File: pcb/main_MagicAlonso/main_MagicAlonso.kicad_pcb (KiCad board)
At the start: 2 copper layers, 3 parts

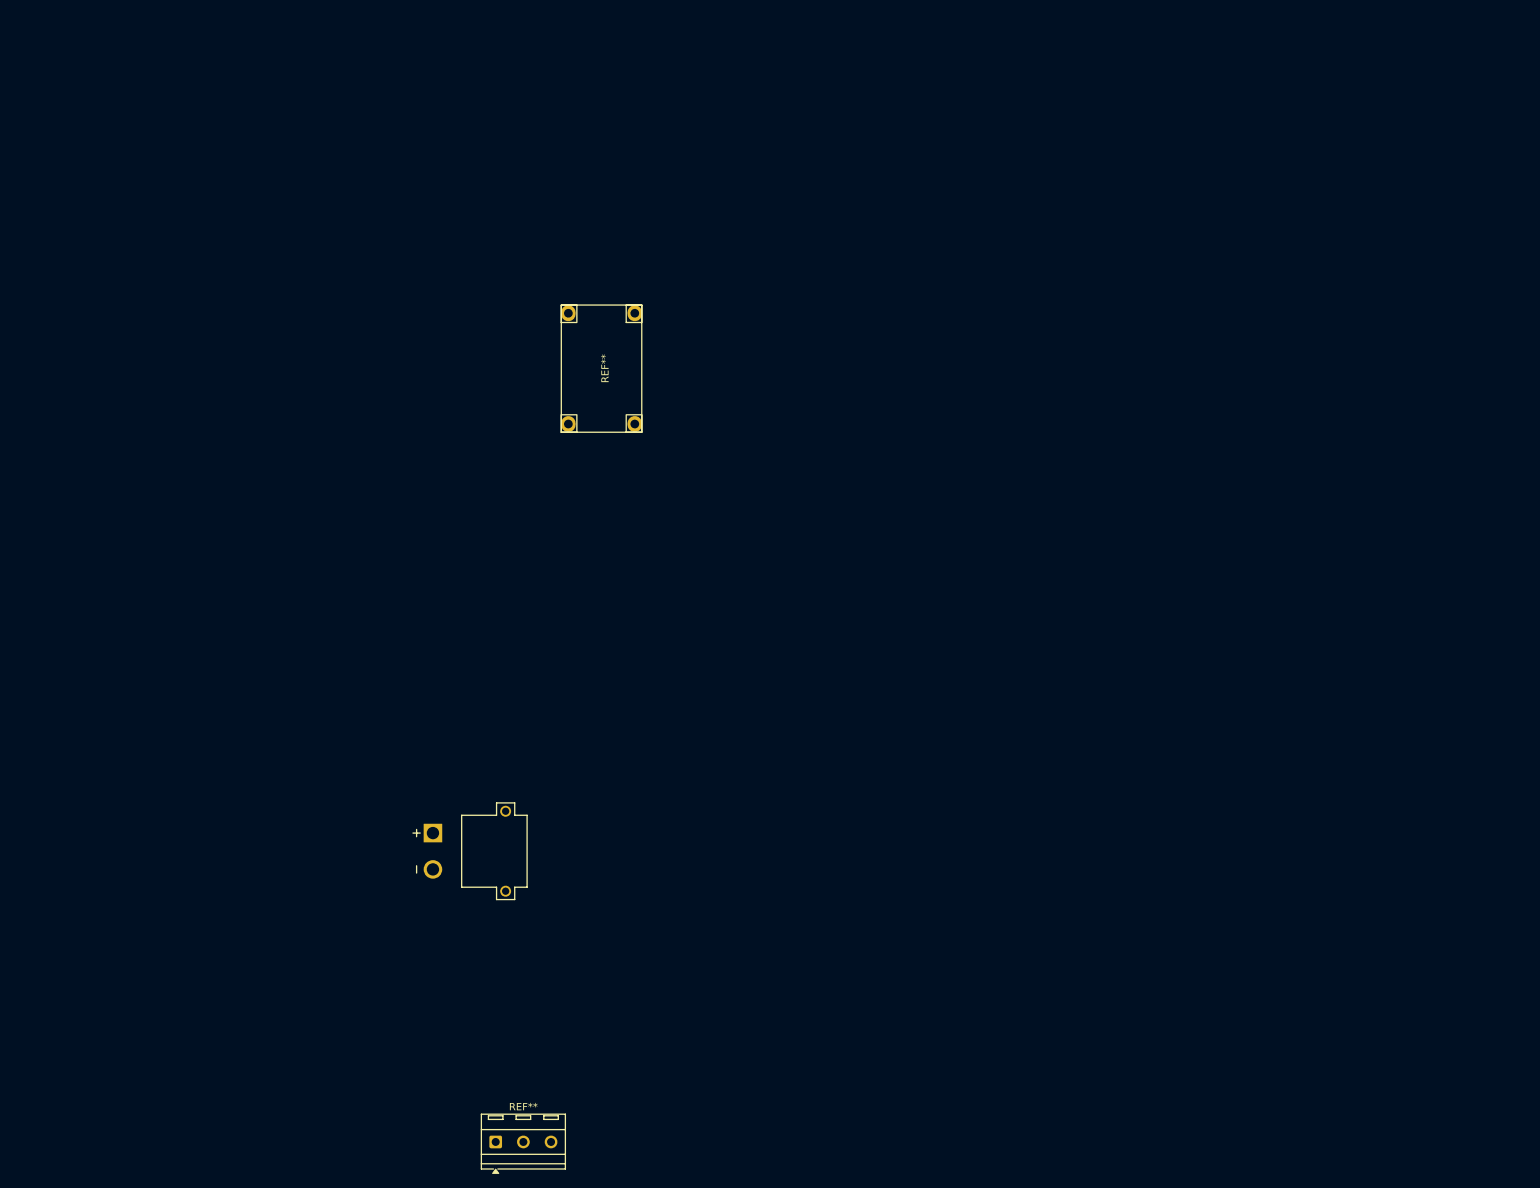
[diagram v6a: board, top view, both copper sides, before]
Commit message: pcb footprint added
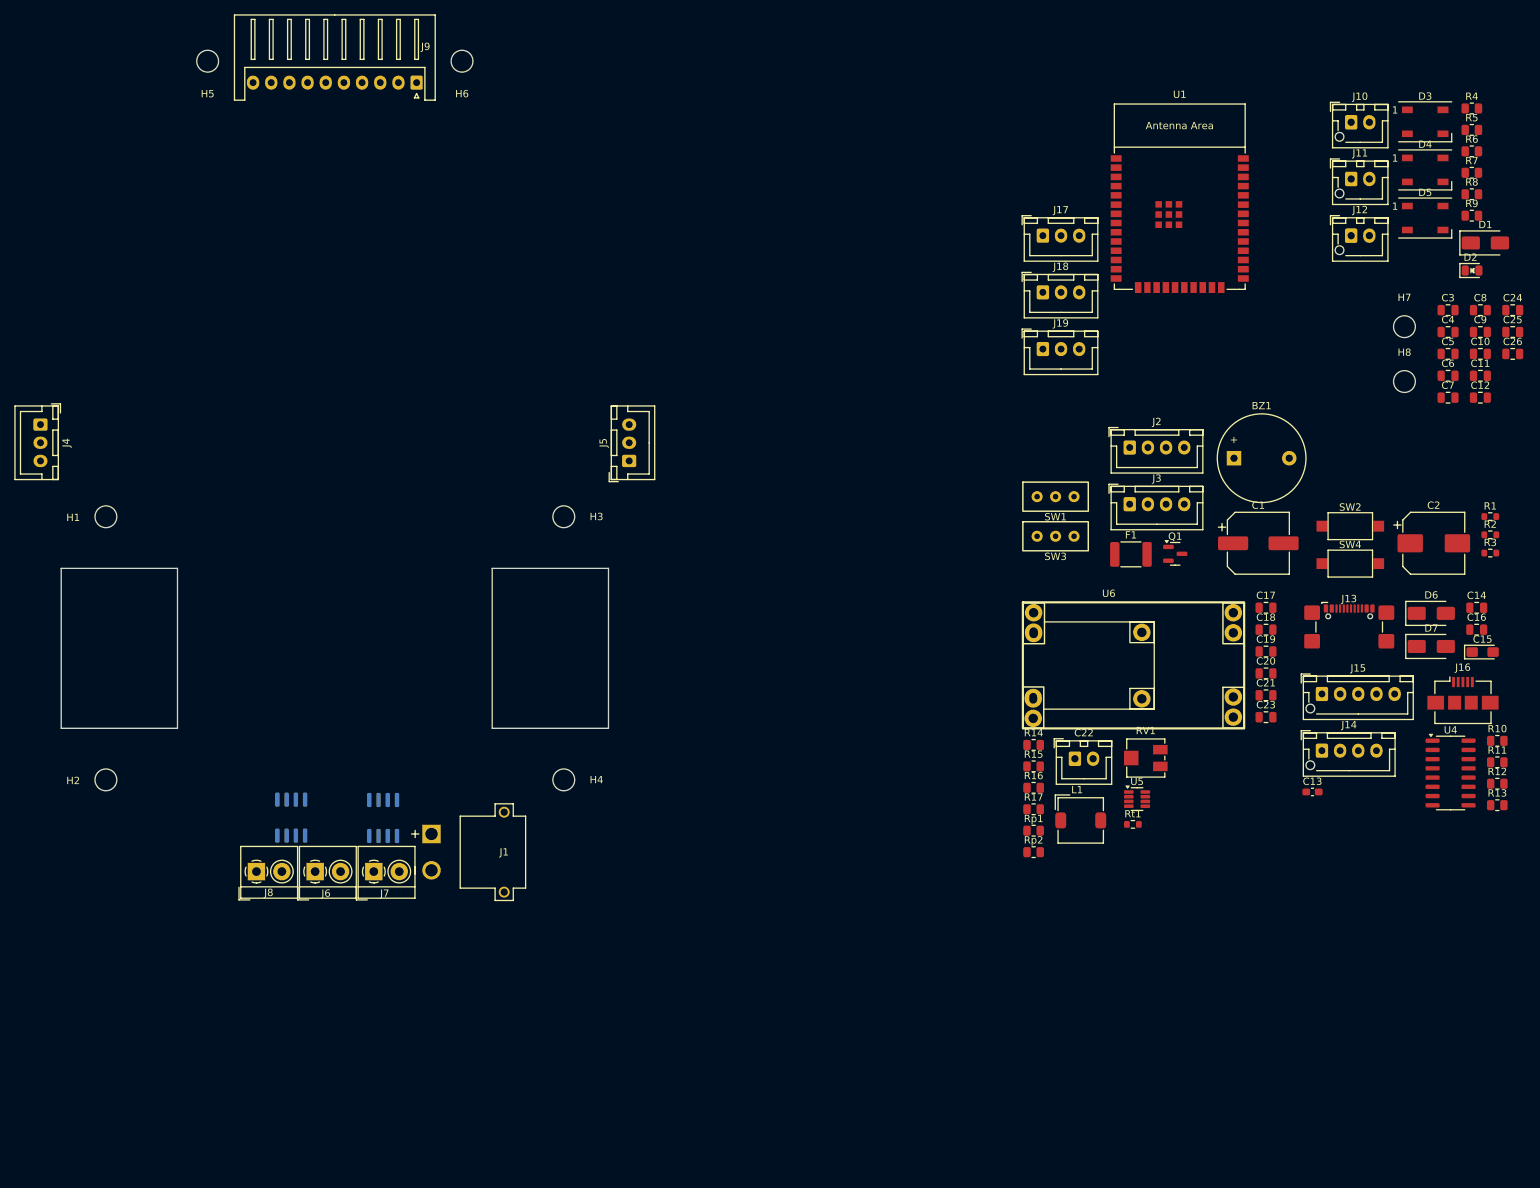
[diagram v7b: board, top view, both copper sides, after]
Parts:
- removed REF**: TerminalBlock_MetzConnect_Type086_RT03403HBLC_1x03_P3.81mm_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, TerminalBlock_MetzConnect:TerminalBlock_MetzConnect_Type086_RT03403HBLC_1x03_P3.81mm_Horizontal
- removed REF**: Mini360, MixLib:Mini360_step-down
- removed REF**: AMASS_XT30PW-M, MixLib:XT30PW-M
- added BZ1: Buzzer, Buzzer_Beeper:Buzzer_12x9.5RM7.6, F.Cu at (230.2, 177.1)
- added C1: 330uF, Capacitor_SMD:CP_Elec_8x11.9, F.Cu at (233.6, 188.8)
- added C10: 10nF, Capacitor_SMD:C_0805_2012Metric, F.Cu at (264.1, 162.8)
- added C11: 1uF, Capacitor_SMD:C_0805_2012Metric, F.Cu at (264.1, 165.8)
- added C12: 100nF, Capacitor_SMD:C_0805_2012Metric, F.Cu at (264.1, 168.8)
- added C13: 1uF, Capacitor_SMD:C_0603_1608Metric_Pad1.08x0.95mm_HandSolder, F.Cu at (241.0, 223.0)
- added C14: 100nF, Capacitor_SMD:C_0805_2012Metric, F.Cu at (263.6, 197.7)
- added C15: 10uF, Capacitor_Tantalum_SMD:CP_EIA-3216-10_Kemet-I_Pad1.58x1.35mm_HandSolder, F.Cu at (264.4, 203.8)
- added C16: 100nF, Capacitor_SMD:C_0805_2012Metric, F.Cu at (263.6, 200.7)
- added C17: 22uF, Capacitor_SMD:C_0805_2012Metric, F.Cu at (234.6, 197.7)
- added C18: 100nF, Capacitor_SMD:C_0805_2012Metric, F.Cu at (234.6, 200.7)
- added C19: 100nF, Capacitor_SMD:C_0805_2012Metric, F.Cu at (234.6, 203.7)
- added C2: 100uF, Capacitor_SMD:CP_Elec_8x10, F.Cu at (257.7, 188.8)
- added C20: 22uF, Capacitor_SMD:C_0805_2012Metric, F.Cu at (234.6, 206.7)
- added C21: 22uF, Capacitor_SMD:C_0805_2012Metric, F.Cu at (234.6, 209.7)
- added C22: 47uF, Connector_JST:JST_XH_B2B-XH-A_1x02_P2.50mm_Vertical, F.Cu at (208.3, 218.5)
- added C23: 100nF, Capacitor_SMD:C_0805_2012Metric, F.Cu at (234.6, 212.8)
- added C24: 100nF, Capacitor_SMD:C_0805_2012Metric, F.Cu at (268.6, 156.8)
- added C25: 100nF, Capacitor_SMD:C_0805_2012Metric, F.Cu at (268.6, 159.8)
- added C26: 100nF, Capacitor_SMD:C_0805_2012Metric, F.Cu at (268.6, 162.8)
- added C3: 1uF, Capacitor_SMD:C_0805_2012Metric, F.Cu at (259.7, 156.8)
- added C4: 100nF, Capacitor_SMD:C_0805_2012Metric, F.Cu at (259.7, 159.8)
- added C5: 100nF, Capacitor_SMD:C_0805_2012Metric, F.Cu at (259.7, 162.8)
- added C6: 100nF, Capacitor_SMD:C_0805_2012Metric, F.Cu at (259.7, 165.8)
- added C7: 100nF, Capacitor_SMD:C_0805_2012Metric, F.Cu at (259.7, 168.8)
- added C8: 100nF, Capacitor_SMD:C_0805_2012Metric, F.Cu at (264.1, 156.8)
- added C9: 10nF, Capacitor_SMD:C_0805_2012Metric, F.Cu at (264.1, 159.8)
- added D1: SS14, Diode_SMD:D_SMA, F.Cu at (264.8, 147.5)
- added D2: LED_On, MixLib:LED_0805_2012Metric, F.Cu at (262.8, 151.3)
- added D3: WS2812B, LED_SMD:LED_WS2812B_PLCC4_5.0x5.0mm_P3.2mm, F.Cu at (256.5, 130.8)
- added D4: WS2812B, LED_SMD:LED_WS2812B_PLCC4_5.0x5.0mm_P3.2mm, F.Cu at (256.5, 137.5)
- added D5: WS2812B, LED_SMD:LED_WS2812B_PLCC4_5.0x5.0mm_P3.2mm, F.Cu at (256.5, 144.1)
- added D6: SS14, Diode_SMD:D_SMA, F.Cu at (257.4, 198.5)
- added D7: SS14, Diode_SMD:D_SMA, F.Cu at (257.4, 203.0)
- added F1: 300mA, Fuse:Fuse_1812_4532Metric_Pad1.30x3.40mm_HandSolder, F.Cu at (216.0, 190.4)
- added H1: M3, MountingHole:MountingHole_3mm, F.Cu at (75.0, 185.2)
- added H2: M3, MountingHole:MountingHole_3mm, F.Cu at (75.0, 221.4)
- added H3: M3, MountingHole:MountingHole_3mm, F.Cu at (138.0, 185.2)
- added H4: M3, MountingHole:MountingHole_3mm, F.Cu at (138.0, 221.4)
- added H5: M3, MountingHole:MountingHole_3mm, F.Cu at (89.0, 122.5)
- added H6: M3, MountingHole:MountingHole_3mm, F.Cu at (124.0, 122.5)
- added H7: M3, MountingHole:MountingHole_3mm, F.Cu at (253.7, 159.0)
- added H8: M3, MountingHole:MountingHole_3mm, F.Cu at (253.7, 166.6)
- added J1: XT30PW-M, MixLib:XT30PW-M, F.Cu at (129.8, 231.3)
- added J10: ESC1, Connector_JST:JST_XH_B2B-XH-AM_1x02_P2.50mm_Vertical, F.Cu at (246.3, 130.9)
- added J11: ESC2, Connector_JST:JST_XH_B2B-XH-AM_1x02_P2.50mm_Vertical, F.Cu at (246.3, 138.7)
- added J12: ESC3, Connector_JST:JST_XH_B2B-XH-AM_1x02_P2.50mm_Vertical, F.Cu at (246.3, 146.5)
- added J13: USB_C_Receptacle_USB2.0_16P, Connector_USB:USB_C_Receptacle_GCT_USB4110, F.Cu at (246.1, 201.5)
- added J14: UART_Out, Connector_JST:JST_XH_B4B-XH-AM_1x04_P2.50mm_Vertical, F.Cu at (242.3, 217.4)
- added J15: USB_Out, Connector_JST:JST_XH_B5B-XH-AM_1x05_P2.50mm_Vertical, F.Cu at (242.3, 209.6)
- added J16: USB_B_Micro, Connector_USB:USB_Micro-B_Amphenol_10104110_Horizontal, F.Cu at (261.7, 209.5)
- added J17: aux0, Connector_JST:JST_XH_B3B-XH-A_1x03_P2.50mm_Vertical, F.Cu at (203.9, 146.5)
- added J18: aux2, Connector_JST:JST_XH_B3B-XH-A_1x03_P2.50mm_Vertical, F.Cu at (203.9, 154.3)
- added J19: aux1, Connector_JST:JST_XH_B3B-XH-A_1x03_P2.50mm_Vertical, F.Cu at (203.9, 162.1)
- added J2: MPU6050, Connector_JST:JST_XH_B4B-XH-A_1x04_P2.50mm_Vertical, F.Cu at (215.9, 175.7)
- added J3: OLED, Connector_JST:JST_XH_B4B-XH-A_1x04_P2.50mm_Vertical, F.Cu at (215.9, 183.5)
- added J4: Encoder1, Connector_JST:JST_XH_B3B-XH-A_1x03_P2.50mm_Vertical, F.Cu at (66.0, 172.5)
- added J5: Encoder2, Connector_JST:JST_XH_B3B-XH-A_1x03_P2.50mm_Vertical, F.Cu at (147.0, 177.5)
- added J6: ESC1_Vb, TerminalBlock_4Ucon:TerminalBlock_4Ucon_1x02_P3.50mm_Horizontal, F.Cu at (103.8, 234.0)
- added J7: ESC2_Vb, TerminalBlock_4Ucon:TerminalBlock_4Ucon_1x02_P3.50mm_Horizontal, F.Cu at (111.9, 234.0)
- added J8: ESC3_Vb, TerminalBlock_4Ucon:TerminalBlock_4Ucon_1x02_P3.50mm_Horizontal, F.Cu at (95.7, 234.0)
- added J9: Sensors, Connector_JST:JST_XH_S10B-XH-A_1x10_P2.50mm_Horizontal, F.Cu at (117.8, 125.5)
- added L1: 6.8uH, Inductor_SMD:L_TDK_SLF6025, F.Cu at (209.1, 227.0)
- added Q1: IRLML2502, Package_TO_SOT_SMD:SOT-23, F.Cu at (222.1, 190.3)
- added R1: 1k, Resistor_SMD:R_0603_1608Metric, F.Cu at (265.5, 185.2)
- added R10: 10k, Resistor_SMD:R_0805_2012Metric, F.Cu at (266.4, 216.0)
- added R11: 10k, Resistor_SMD:R_0805_2012Metric, F.Cu at (266.4, 219.0)
- added R12: 10k, Resistor_SMD:R_0805_2012Metric, F.Cu at (266.4, 221.9)
- added R13: 10k, Resistor_SMD:R_0805_2012Metric, F.Cu at (266.4, 224.9)
- added R14: 20, Resistor_SMD:R_0805_2012Metric, F.Cu at (202.6, 216.6)
- added R15: 100k, Resistor_SMD:R_0805_2012Metric, F.Cu at (202.6, 219.5)
- added R16: 10k, Resistor_SMD:R_0805_2012Metric, F.Cu at (202.6, 222.5)
- added R17: 10k, Resistor_SMD:R_0805_2012Metric, F.Cu at (202.6, 225.4)
- added R2: 10k, Resistor_SMD:R_0603_1608Metric, F.Cu at (265.5, 187.7)
- added R3: 10k, Resistor_SMD:R_0603_1608Metric, F.Cu at (265.5, 190.2)
- added R4: 330, Resistor_SMD:R_0805_2012Metric, F.Cu at (262.9, 129.0)
- added R5: 100, Resistor_SMD:R_0805_2012Metric, F.Cu at (262.9, 132.0)
- added R6: 100, Resistor_SMD:R_0805_2012Metric, F.Cu at (262.9, 134.9)
- added R7: 100, Resistor_SMD:R_0805_2012Metric, F.Cu at (262.9, 137.9)
- added R8: 330, Resistor_SMD:R_0805_2012Metric, F.Cu at (262.9, 140.8)
- added R9: 10k, Resistor_SMD:R_0805_2012Metric, F.Cu at (262.9, 143.8)
- added RV1: Pot, Potentiometer_SMD:Potentiometer_Vishay_TS53YJ_Vertical, F.Cu at (218.1, 218.4)
- added Rp1: 47k, Resistor_SMD:R_0805_2012Metric, F.Cu at (202.6, 228.4)
- added Rp2: 100k, Resistor_SMD:R_0805_2012Metric, F.Cu at (202.6, 231.3)
- added Rt1: 33k, Resistor_SMD:R_0603_1608Metric, F.Cu at (216.3, 227.5)
- added SW1: Power_SW, MixLib:SW_Slide-03_P2.54_L9_W4_H7, F.Cu at (205.7, 182.4)
- added SW2: EN_Push, Button_Switch_SMD:SW_SPST_CK_RS282G05A3, F.Cu at (246.2, 186.5)
- added SW3: Boot_SW, MixLib:SW_Slide-03_P2.54_L9_W4_H7, F.Cu at (205.7, 187.9)
- added SW4: BUTTON_Push, Button_Switch_SMD:SW_SPST_CK_RS282G05A3, F.Cu at (246.2, 191.6)
- added U1: ESP32-WROOM-32E, PCM_Espressif:ESP32-WROOM-32E, F.Cu at (222.8, 142.9)
- added U2: ACS712-30A, Package_SO:SOIC-8_3.9x4.9mm_P1.27mm, B.Cu at (113.1, 226.6)
- added U3: ACS712-20A, Package_SO:SOIC-8_3.9x4.9mm_P1.27mm, B.Cu at (100.5, 226.6)
- added U4: CH340C, Package_SO:SOIC-16_3.9x9.9mm_P1.27mm, F.Cu at (260.0, 220.4)
- added U5: MP2315, Package_TO_SOT_SMD:TSOT-23-8, F.Cu at (216.9, 224.0)
- added U6: Mini360-MP4560, MixLib:Mix_Mini360-MP4560, F.Cu at (215.8, 205.5)
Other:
- board outline added: 75.3 x 22 mm
- board text added: "BLS 2130 55A 4IN1 ESC"

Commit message: pcb components & label fixes
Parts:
- removed U5: MP2315, Package_TO_SOT_SMD:TSOT-23-8
- added ST1: MP2315, Package_TO_SOT_SMD:TSOT-23-8, F.Cu at (252.8, 135.2)
- C1: footprint Capacitor_SMD:CP_Elec_8x11.9 -> Capacitor_THT:CP_Radial_D8.0mm_P3.80mm
- C15: footprint Capacitor_Tantalum_SMD:CP_EIA-3216-10_Kemet-I_Pad1.58x1.35mm_HandSolder -> Capacitor_Tantalum_SMD:CP_EIA-3216-10_Kemet-I_HandSolder
- C2: footprint Capacitor_SMD:CP_Elec_8x10 -> Capacitor_SMD:CP_Elec_6.3x5.4
- C22: footprint Connector_JST:JST_XH_B2B-XH-A_1x02_P2.50mm_Vertical -> Capacitor_SMD:CP_Elec_6.3x5.4
- J10, J11, J12: footprint Connector_JST:JST_XH_B2B-XH-AM_1x02_P2.50mm_Vertical -> Connector_JST:JST_XH_B2B-XH-A_1x02_P2.50mm_Vertical
- J14: footprint Connector_JST:JST_XH_B4B-XH-AM_1x04_P2.50mm_Vertical -> Connector_JST:JST_XH_B4B-XH-A_1x04_P2.50mm_Vertical
- J15: footprint Connector_JST:JST_XH_B5B-XH-AM_1x05_P2.50mm_Vertical -> Connector_PinSocket_2.54mm:PinSocket_1x05_P2.54mm_Vertical
- J6: value ESC1_Vb -> ESC1_VM
- J7: value ESC2_Vb -> ESC2_VM
- J8: value ESC3_Vb -> ESC3_VM
- U6: value Mini360-MP4560 -> Mini360; footprint MixLib:Mix_Mini360-MP4560 -> MixLib:Mini360_step-down
- moved C5 242.1 mm to (18.1, 147.2)
- moved C6 242.1 mm to (18.1, 150.3)
- moved C7 242.1 mm to (18.1, 153.3)
- moved C10 242.1 mm to (22.6, 147.2)
- moved C8 242.1 mm to (22.6, 141.2)
- moved C9 242.1 mm to (22.6, 144.2)
- moved R1 240.1 mm to (26.0, 168.2)
- moved R2 240.1 mm to (26.0, 170.7)
- moved R3 240.1 mm to (26.0, 173.2)
- moved C4 198.7 mm to (61.2, 170.4), turned to -90 degrees
- moved C3 196.9 mm to (63.2, 170.4), turned to -90 degrees
- moved C12 171.9 mm to (96.5, 130.4), turned to 180 degrees
- moved SW2 171.6 mm to (75.4, 170.3), turned to 180 degrees
- moved C11 170.7 mm to (96.5, 133.4), turned to 180 degrees
- moved F1 168.5 mm to (49.8, 162.8), turned to -90 degrees
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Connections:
- net /CH340C/Vbus renamed /CH340C/VMus
- net /CH340C/VbusB renamed /CH340C/VMusB
- net /CH340C/VbusC renamed /CH340C/VMusC
- net /ESC1&2_Vb renamed /ESC1&2_VM
- net /ESC3_Vb renamed /ESC3_VM
- net Net-(U5-SW) renamed /StepDown_2315/SW
- net Net-(U5-VCC) renamed /StepDown_2315/VCC_MP
- C1 pad 1: /Vb -> /VM
- C15 pad 2: /Vusb -> /Vb
- C16 pad 2: /Vusb -> /Vb
- C17 pad 1: /Vusb -> /Vb
- C18 pad 1: /Vusb -> /Vb
- C2 pad 1: /Vb -> /VM
- C24 pad 1: +3.3V -> Net-(D3-VDD)
- C24 pad 2: Net-(D3-VDD) -> GND
- C25 pad 1: +3.3V -> Net-(D4-VDD)
- C25 pad 2: Net-(D4-VDD) -> GND
- C26 pad 1: +3.3V -> Net-(D5-VDD)
- C26 pad 2: Net-(D5-VDD) -> GND
- D1 pad 1: /Vusb -> /Vb
- D6 pad 1: /Vusb -> /Vb
- D7 pad 1: /Vusb -> /Vb
- J1 pad P: /Vb -> /VM
- R14 pad 2: Net-(U5-BST) -> /StepDown_2315/BST
- R15 pad 2: /Vusb -> /Vb
- R16 pad 1: Net-(U5-AAM) -> /StepDown_2315/AAM
- R4 pad 2: /Vb -> /VM
- Rt1 pad 1: Net-(U5-FB) -> /StepDown_2315/FB
- SW1 pad 1: /Vb -> /VM
- U2 pad 1: /Vb -> /VM
- U2 pad 2: /Vb -> /VM
- U3 pad 1: /Vb -> /VM
- U3 pad 2: /Vb -> /VM
- U6 pad 1: /Vusb -> /Vb
- U6 pad 2: /Vusb -> GND
- U6 pad 3: GND -> +3.3V
